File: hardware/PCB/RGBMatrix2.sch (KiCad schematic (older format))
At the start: 29 parts

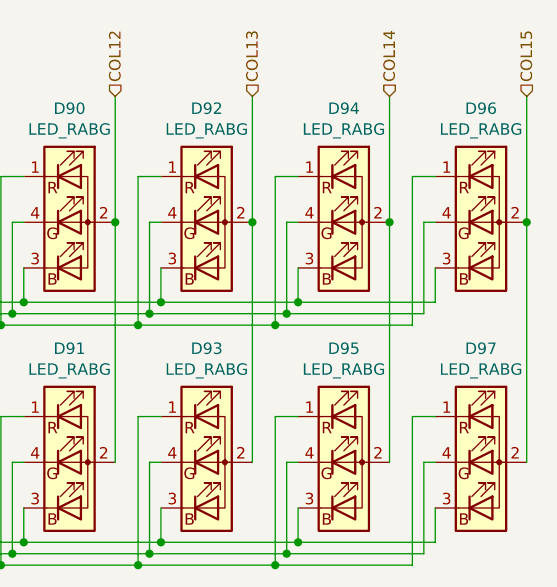
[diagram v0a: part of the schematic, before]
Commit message: Line up most parts and fix some problems with the part
1.Fix the LED footprint size
2.Edit the hotplug to be simpler (removed 2 holes)
3.Line up everything and the silkscreen
4. Fix the LED matrix and the switch matrix sch
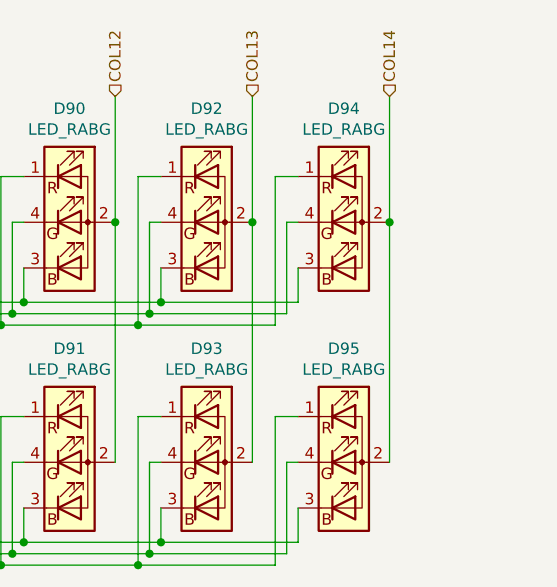
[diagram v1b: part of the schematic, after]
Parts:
- removed D96, D97: LED_RABG, KiCad:XZMDKCBDDG45S9, symbol Device:LED_RABG
- D69, D70, D71, D72, D73, D74, D75, D76, D77, D78, D79, D80, D81, D82, D83, D84, D85, D86, D87, D88, D89, D90, D91, D92, D93, D94, D95: footprint KiCad:XZMDKCBDDG45S9 -> KiCad:XZMDKCBDDG45S9_fixed

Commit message: alot of changes
modify the QFN-48 so PCB 3d view in future would look better (so I don't design a part that doesn't fit)
I made a useless QFN-40 3d model
modify schematics so it looks better
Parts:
- D69, D70, D71, D72, D73, D74, D75, D76, D77, D78, D79, D80, D81, D82, D83, D84, D85, D86, D87, D88, D89, D90, D91, D92, D93, D94, D95: Footprint (none) -> KiCad:XZMDKCBDDG45S9_fixed; Value (none) -> XZMDKCBDDG45S9
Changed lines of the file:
@@
 encoding utf-8
 Sheet 4 6
-Title ""
-Date ""
-Rev ""
+Title "NHW68"
+Date "2020-01-28"
+Rev "0.1"
 Comp ""
 Comment1 ""
@@
 F 2 "KiCad:XZMDKCBDDG45S9_fixed" H 1750 2350 50  0001 C CNN
 F 3 "~" H 1750 2350 50  0001 C CNN
+F 4 "KiCad:XZMDKCBDDG45S9_fixed" H 1750 2400 50  0001 C CNN "Footprint"
+F 5 "XZMDKCBDDG45S9" H 1750 2400 50  0001 C CNN "Value"
 	1    1750 2400
 	1    0    0    -1
@@
 F 2 "KiCad:XZMDKCBDDG45S9_fixed" H 2350 2350 50  0001 C CNN
 F 3 "~" H 2350 2350 50  0001 C CNN
+F 4 "KiCad:XZMDKCBDDG45S9_fixed" H 2350 2400 50  0001 C CNN "Footprint"
+F 5 "XZMDKCBDDG45S9" H 2350 2400 50  0001 C CNN "Value"
 	1    2350 2400
 	1    0    0    -1
@@
 F 2 "KiCad:XZMDKCBDDG45S9_fixed" H 2950 2350 50  0001 C CNN
 F 3 "~" H 2950 2350 50  0001 C CNN
+F 4 "KiCad:XZMDKCBDDG45S9_fixed" H 2950 2400 50  0001 C CNN "Footprint"
+F 5 "XZMDKCBDDG45S9" H 2950 2400 50  0001 C CNN "Value"
 	1    2950 2400
 	1    0    0    -1
@@
 F 2 "KiCad:XZMDKCBDDG45S9_fixed" H 3550 2350 50  0001 C CNN
 F 3 "~" H 3550 2350 50  0001 C CNN
+F 4 "KiCad:XZMDKCBDDG45S9_fixed" H 3550 2400 50  0001 C CNN "Footprint"
+F 5 "XZMDKCBDDG45S9" H 3550 2400 50  0001 C CNN "Value"
 	1    3550 2400
 	1    0    0    -1
@@
 F 2 "KiCad:XZMDKCBDDG45S9_fixed" H 4100 2350 50  0001 C CNN
 F 3 "~" H 4100 2350 50  0001 C CNN
+F 4 "KiCad:XZMDKCBDDG45S9_fixed" H 4100 2400 50  0001 C CNN "Footprint"
+F 5 "XZMDKCBDDG45S9" H 4100 2400 50  0001 C CNN "Value"
 	1    4100 2400
 	1    0    0    -1
@@
 F 2 "KiCad:XZMDKCBDDG45S9_fixed" H 4700 2350 50  0001 C CNN
 F 3 "~" H 4700 2350 50  0001 C CNN
+F 4 "KiCad:XZMDKCBDDG45S9_fixed" H 4700 2400 50  0001 C CNN "Footprint"
+F 5 "XZMDKCBDDG45S9" H 4700 2400 50  0001 C CNN "Value"
 	1    4700 2400
 	1    0    0    -1
@@
 F 2 "KiCad:XZMDKCBDDG45S9_fixed" H 5300 2350 50  0001 C CNN
 F 3 "~" H 5300 2350 50  0001 C CNN
+F 4 "KiCad:XZMDKCBDDG45S9_fixed" H 5300 2400 50  0001 C CNN "Footprint"
+F 5 "XZMDKCBDDG45S9" H 5300 2400 50  0001 C CNN "Value"
 	1    5300 2400
 	1    0    0    -1
@@
 F 2 "KiCad:XZMDKCBDDG45S9_fixed" H 5900 2350 50  0001 C CNN
 F 3 "~" H 5900 2350 50  0001 C CNN
+F 4 "KiCad:XZMDKCBDDG45S9_fixed" H 5900 2400 50  0001 C CNN "Footprint"
+F 5 "XZMDKCBDDG45S9" H 5900 2400 50  0001 C CNN "Value"
 	1    5900 2400
 	1    0    0    -1
@@
 F 2 "KiCad:XZMDKCBDDG45S9_fixed" H 6500 2350 50  0001 C CNN
 F 3 "~" H 6500 2350 50  0001 C CNN
+F 4 "KiCad:XZMDKCBDDG45S9_fixed" H 6500 2400 50  0001 C CNN "Footprint"
+F 5 "XZMDKCBDDG45S9" H 6500 2400 50  0001 C CNN "Value"
 	1    6500 2400
 	1    0    0    -1
@@
 F 2 "KiCad:XZMDKCBDDG45S9_fixed" H 7100 2350 50  0001 C CNN
 F 3 "~" H 7100 2350 50  0001 C CNN
+F 4 "KiCad:XZMDKCBDDG45S9_fixed" H 7100 2400 50  0001 C CNN "Footprint"
+F 5 "XZMDKCBDDG45S9" H 7100 2400 50  0001 C CNN "Value"
 	1    7100 2400
 	1    0    0    -1
@@
 F 2 "KiCad:XZMDKCBDDG45S9_fixed" H 7700 2350 50  0001 C CNN
 F 3 "~" H 7700 2350 50  0001 C CNN
+F 4 "KiCad:XZMDKCBDDG45S9_fixed" H 7700 2400 50  0001 C CNN "Footprint"
+F 5 "XZMDKCBDDG45S9" H 7700 2400 50  0001 C CNN "Value"
 	1    7700 2400
 	1    0    0    -1
@@
 F 2 "KiCad:XZMDKCBDDG45S9_fixed" H 8300 2350 50  0001 C CNN
 F 3 "~" H 8300 2350 50  0001 C CNN
+F 4 "KiCad:XZMDKCBDDG45S9_fixed" H 8300 2400 50  0001 C CNN "Footprint"
+F 5 "XZMDKCBDDG45S9" H 8300 2400 50  0001 C CNN "Value"
 	1    8300 2400
 	1    0    0    -1
@@
 F 2 "KiCad:XZMDKCBDDG45S9_fixed" H 8900 2350 50  0001 C CNN
 F 3 "~" H 8900 2350 50  0001 C CNN
+F 4 "KiCad:XZMDKCBDDG45S9_fixed" H 8900 2400 50  0001 C CNN "Footprint"
+F 5 "XZMDKCBDDG45S9" H 8900 2400 50  0001 C CNN "Value"
 	1    8900 2400
 	1    0    0    -1
@@
 F 2 "KiCad:XZMDKCBDDG45S9_fixed" H 9500 2350 50  0001 C CNN
 F 3 "~" H 9500 2350 50  0001 C CNN
+F 4 "KiCad:XZMDKCBDDG45S9_fixed" H 9500 2400 50  0001 C CNN "Footprint"
+F 5 "XZMDKCBDDG45S9" H 9500 2400 50  0001 C CNN "Value"
 	1    9500 2400
 	1    0    0    -1
@@
 F 2 "KiCad:XZMDKCBDDG45S9_fixed" H 9500 3400 50  0001 C CNN
 F 3 "~" H 9500 3400 50  0001 C CNN
+F 4 "KiCad:XZMDKCBDDG45S9_fixed" H 9500 3450 50  0001 C CNN "Footprint"
+F 5 "XZMDKCBDDG45S9" H 9500 3450 50  0001 C CNN "Value"
 	1    9500 3450
 	1    0    0    -1
@@
 F 2 "KiCad:XZMDKCBDDG45S9_fixed" H 8300 3400 50  0001 C CNN
 F 3 "~" H 8300 3400 50  0001 C CNN
+F 4 "KiCad:XZMDKCBDDG45S9_fixed" H 8300 3450 50  0001 C CNN "Footprint"
+F 5 "XZMDKCBDDG45S9" H 8300 3450 50  0001 C CNN "Value"
 	1    8300 3450
 	1    0    0    -1
@@
 F 2 "KiCad:XZMDKCBDDG45S9_fixed" H 7700 3400 50  0001 C CNN
 F 3 "~" H 7700 3400 50  0001 C CNN
+F 4 "KiCad:XZMDKCBDDG45S9_fixed" H 7700 3450 50  0001 C CNN "Footprint"
+F 5 "XZMDKCBDDG45S9" H 7700 3450 50  0001 C CNN "Value"
 	1    7700 3450
 	1    0    0    -1
@@
 F 2 "KiCad:XZMDKCBDDG45S9_fixed" H 7100 3400 50  0001 C CNN
 F 3 "~" H 7100 3400 50  0001 C CNN
+F 4 "KiCad:XZMDKCBDDG45S9_fixed" H 7100 3450 50  0001 C CNN "Footprint"
+F 5 "XZMDKCBDDG45S9" H 7100 3450 50  0001 C CNN "Value"
 	1    7100 3450
 	1    0    0    -1
@@
 F 2 "KiCad:XZMDKCBDDG45S9_fixed" H 6500 3400 50  0001 C CNN
 F 3 "~" H 6500 3400 50  0001 C CNN
+F 4 "KiCad:XZMDKCBDDG45S9_fixed" H 6500 3450 50  0001 C CNN "Footprint"
+F 5 "XZMDKCBDDG45S9" H 6500 3450 50  0001 C CNN "Value"
 	1    6500 3450
 	1    0    0    -1
@@
 F 2 "KiCad:XZMDKCBDDG45S9_fixed" H 5900 3400 50  0001 C CNN
 F 3 "~" H 5900 3400 50  0001 C CNN
+F 4 "KiCad:XZMDKCBDDG45S9_fixed" H 5900 3450 50  0001 C CNN "Footprint"
+F 5 "XZMDKCBDDG45S9" H 5900 3450 50  0001 C CNN "Value"
 	1    5900 3450
 	1    0    0    -1
@@
 F 2 "KiCad:XZMDKCBDDG45S9_fixed" H 4700 3400 50  0001 C CNN
 F 3 "~" H 4700 3400 50  0001 C CNN
+F 4 "KiCad:XZMDKCBDDG45S9_fixed" H 4700 3450 50  0001 C CNN "Footprint"
+F 5 "XZMDKCBDDG45S9" H 4700 3450 50  0001 C CNN "Value"
 	1    4700 3450
 	1    0    0    -1
@@
 F 2 "KiCad:XZMDKCBDDG45S9_fixed" H 4100 3400 50  0001 C CNN
 F 3 "~" H 4100 3400 50  0001 C CNN
+F 4 "KiCad:XZMDKCBDDG45S9_fixed" H 4100 3450 50  0001 C CNN "Footprint"
+F 5 "XZMDKCBDDG45S9" H 4100 3450 50  0001 C CNN "Value"
 	1    4100 3450
 	1    0    0    -1
@@
 F 2 "KiCad:XZMDKCBDDG45S9_fixed" H 3550 3400 50  0001 C CNN
 F 3 "~" H 3550 3400 50  0001 C CNN
+F 4 "KiCad:XZMDKCBDDG45S9_fixed" H 3550 3450 50  0001 C CNN "Footprint"
+F 5 "XZMDKCBDDG45S9" H 3550 3450 50  0001 C CNN "Value"
 	1    3550 3450
 	1    0    0    -1
@@
 F 2 "KiCad:XZMDKCBDDG45S9_fixed" H 2950 3400 50  0001 C CNN
 F 3 "~" H 2950 3400 50  0001 C CNN
+F 4 "KiCad:XZMDKCBDDG45S9_fixed" H 2950 3450 50  0001 C CNN "Footprint"
+F 5 "XZMDKCBDDG45S9" H 2950 3450 50  0001 C CNN "Value"
 	1    2950 3450
 	1    0    0    -1
@@
 F 2 "KiCad:XZMDKCBDDG45S9_fixed" H 2350 3400 50  0001 C CNN
 F 3 "~" H 2350 3400 50  0001 C CNN
+F 4 "KiCad:XZMDKCBDDG45S9_fixed" H 2350 3450 50  0001 C CNN "Footprint"
+F 5 "XZMDKCBDDG45S9" H 2350 3450 50  0001 C CNN "Value"
 	1    2350 3450
 	1    0    0    -1
@@
 F 2 "KiCad:XZMDKCBDDG45S9_fixed" H 1750 3400 50  0001 C CNN
 F 3 "~" H 1750 3400 50  0001 C CNN
+F 4 "KiCad:XZMDKCBDDG45S9_fixed" H 1750 3450 50  0001 C CNN "Footprint"
+F 5 "XZMDKCBDDG45S9" H 1750 3450 50  0001 C CNN "Value"
 	1    1750 3450
 	1    0    0    -1
@@
 F 2 "KiCad:XZMDKCBDDG45S9_fixed" H 8900 3400 50  0001 C CNN
 F 3 "~" H 8900 3400 50  0001 C CNN
+F 4 "KiCad:XZMDKCBDDG45S9_fixed" H 8900 3450 50  0001 C CNN "Footprint"
+F 5 "XZMDKCBDDG45S9" H 8900 3450 50  0001 C CNN "Value"
 	1    8900 3450
 	1    0    0    -1

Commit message: making progress
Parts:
- D69, D70, D71, D72, D73, D74, D75, D76, D77, D78, D79, D80, D81, D82, D83, D84, D85, D86, D87, D88, D89, D90, D91, D92, D93, D94, D95: value LED_RABG -> XZMDKCBDDG45S-9
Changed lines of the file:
@@
 AR Path="/5EC33E3D/5E12F961/5ECE6F4E" Ref="D69"  Part="1"
 F 0 "D69" H 1750 2897 50  0000 C CNN
-F 1 "LED_RABG" H 1750 2806 50  0000 C CNN
+F 1 "XZMDKCBDDG45S-9" H 1750 2806 50  0000 C CNN
 F 2 "KiCad:XZMDKCBDDG45S9_fixed" H 1750 2350 50  0001 C CNN
 F 3 "~" H 1750 2350 50  0001 C CNN
@@
 AR Path="/5EC33E3D/5E12F961/5ECF7D8D" Ref="D71"  Part="1"
 F 0 "D71" H 2350 2897 50  0000 C CNN
-F 1 "LED_RABG" H 2350 2806 50  0000 C CNN
+F 1 "XZMDKCBDDG45S-9" H 2350 2806 50  0000 C CNN
 F 2 "KiCad:XZMDKCBDDG45S9_fixed" H 2350 2350 50  0001 C CNN
 F 3 "~" H 2350 2350 50  0001 C CNN
@@
 AR Path="/5EC33E3D/5E12F961/5ED08C1C" Ref="D73"  Part="1"
 F 0 "D73" H 2950 2897 50  0000 C CNN
-F 1 "LED_RABG" H 2950 2806 50  0000 C CNN
+F 1 "XZMDKCBDDG45S-9" H 2950 2806 50  0000 C CNN
 F 2 "KiCad:XZMDKCBDDG45S9_fixed" H 2950 2350 50  0001 C CNN
 F 3 "~" H 2950 2350 50  0001 C CNN
@@
 AR Path="/5EC33E3D/5E12F961/5ED19532" Ref="D75"  Part="1"
 F 0 "D75" H 3550 2897 50  0000 C CNN
-F 1 "LED_RABG" H 3550 2806 50  0000 C CNN
+F 1 "XZMDKCBDDG45S-9" H 3550 2806 50  0000 C CNN
 F 2 "KiCad:XZMDKCBDDG45S9_fixed" H 3550 2350 50  0001 C CNN
 F 3 "~" H 3550 2350 50  0001 C CNN
@@
 AR Path="/5EC33E3D/5E12F961/5ED2A1D2" Ref="D77"  Part="1"
 F 0 "D77" H 4100 2897 50  0000 C CNN
-F 1 "LED_RABG" H 4100 2806 50  0000 C CNN
+F 1 "XZMDKCBDDG45S-9" H 4100 2806 50  0000 C CNN
 F 2 "KiCad:XZMDKCBDDG45S9_fixed" H 4100 2350 50  0001 C CNN
 F 3 "~" H 4100 2350 50  0001 C CNN
@@
 AR Path="/5EC33E3D/5E12F961/5ED3AE35" Ref="D79"  Part="1"
 F 0 "D79" H 4700 2897 50  0000 C CNN
-F 1 "LED_RABG" H 4700 2806 50  0000 C CNN
+F 1 "XZMDKCBDDG45S-9" H 4700 2806 50  0000 C CNN
 F 2 "KiCad:XZMDKCBDDG45S9_fixed" H 4700 2350 50  0001 C CNN
 F 3 "~" H 4700 2350 50  0001 C CNN
@@
 AR Path="/5EC33E3D/5E12F961/5ED4B8F9" Ref="D81"  Part="1"
 F 0 "D81" H 5300 2897 50  0000 C CNN
-F 1 "LED_RABG" H 5300 2806 50  0000 C CNN
+F 1 "XZMDKCBDDG45S-9" H 5300 2806 50  0000 C CNN
 F 2 "KiCad:XZMDKCBDDG45S9_fixed" H 5300 2350 50  0001 C CNN
 F 3 "~" H 5300 2350 50  0001 C CNN
@@
 AR Path="/5EC33E3D/5E12F961/5ED5C37B" Ref="D82"  Part="1"
 F 0 "D82" H 5900 2897 50  0000 C CNN
-F 1 "LED_RABG" H 5900 2806 50  0000 C CNN
+F 1 "XZMDKCBDDG45S-9" H 5900 2806 50  0000 C CNN
 F 2 "KiCad:XZMDKCBDDG45S9_fixed" H 5900 2350 50  0001 C CNN
 F 3 "~" H 5900 2350 50  0001 C CNN
@@
 AR Path="/5EC33E3D/5E12F961/5ED6CA4B" Ref="D84"  Part="1"
 F 0 "D84" H 6500 2897 50  0000 C CNN
-F 1 "LED_RABG" H 6500 2806 50  0000 C CNN
+F 1 "XZMDKCBDDG45S-9" H 6500 2806 50  0000 C CNN
 F 2 "KiCad:XZMDKCBDDG45S9_fixed" H 6500 2350 50  0001 C CNN
 F 3 "~" H 6500 2350 50  0001 C CNN
@@
 AR Path="/5EC33E3D/5E12F961/5ED7D671" Ref="D86"  Part="1"
 F 0 "D86" H 7100 2897 50  0000 C CNN
-F 1 "LED_RABG" H 7100 2806 50  0000 C CNN
+F 1 "XZMDKCBDDG45S-9" H 7100 2806 50  0000 C CNN
 F 2 "KiCad:XZMDKCBDDG45S9_fixed" H 7100 2350 50  0001 C CNN
 F 3 "~" H 7100 2350 50  0001 C CNN
@@
 AR Path="/5EC33E3D/5E12F961/5ED8E3BC" Ref="D88"  Part="1"
 F 0 "D88" H 7700 2897 50  0000 C CNN
-F 1 "LED_RABG" H 7700 2806 50  0000 C CNN
+F 1 "XZMDKCBDDG45S-9" H 7700 2806 50  0000 C CNN
 F 2 "KiCad:XZMDKCBDDG45S9_fixed" H 7700 2350 50  0001 C CNN
 F 3 "~" H 7700 2350 50  0001 C CNN
@@
 AR Path="/5EC33E3D/5E12F961/5ED9EECC" Ref="D90"  Part="1"
 F 0 "D90" H 8300 2897 50  0000 C CNN
-F 1 "LED_RABG" H 8300 2806 50  0000 C CNN
+F 1 "XZMDKCBDDG45S-9" H 8300 2806 50  0000 C CNN
 F 2 "KiCad:XZMDKCBDDG45S9_fixed" H 8300 2350 50  0001 C CNN
 F 3 "~" H 8300 2350 50  0001 C CNN
@@
 AR Path="/5EC33E3D/5E12F961/5EDAF8D0" Ref="D92"  Part="1"
 F 0 "D92" H 8900 2897 50  0000 C CNN
-F 1 "LED_RABG" H 8900 2806 50  0000 C CNN
+F 1 "XZMDKCBDDG45S-9" H 8900 2806 50  0000 C CNN
 F 2 "KiCad:XZMDKCBDDG45S9_fixed" H 8900 2350 50  0001 C CNN
 F 3 "~" H 8900 2350 50  0001 C CNN
@@
 AR Path="/5EC33E3D/5E12F961/5EDC0468" Ref="D94"  Part="1"
 F 0 "D94" H 9500 2897 50  0000 C CNN
-F 1 "LED_RABG" H 9500 2806 50  0000 C CNN
+F 1 "XZMDKCBDDG45S-9" H 9500 2806 50  0000 C CNN
 F 2 "KiCad:XZMDKCBDDG45S9_fixed" H 9500 2350 50  0001 C CNN
 F 3 "~" H 9500 2350 50  0001 C CNN
@@
 AR Path="/5EC33E3D/5E12F961/5EDF2634" Ref="D95"  Part="1"
 F 0 "D95" H 9500 3947 50  0000 C CNN
-F 1 "LED_RABG" H 9500 3856 50  0000 C CNN
+F 1 "XZMDKCBDDG45S-9" H 9500 3856 50  0000 C CNN
 F 2 "KiCad:XZMDKCBDDG45S9_fixed" H 9500 3400 50  0001 C CNN
 F 3 "~" H 9500 3400 50  0001 C CNN
@@
 AR Path="/5EC33E3D/5E12F961/5EE13AA6" Ref="D91"  Part="1"
 F 0 "D91" H 8300 3947 50  0000 C CNN
-F 1 "LED_RABG" H 8300 3856 50  0000 C CNN
+F 1 "XZMDKCBDDG45S-9" H 8300 3856 50  0000 C CNN
 F 2 "KiCad:XZMDKCBDDG45S9_fixed" H 8300 3400 50  0001 C CNN
 F 3 "~" H 8300 3400 50  0001 C CNN
@@
 AR Path="/5EC33E3D/5E12F961/5EE24547" Ref="D89"  Part="1"
 F 0 "D89" H 7700 3947 50  0000 C CNN
-F 1 "LED_RABG" H 7700 3856 50  0000 C CNN
+F 1 "XZMDKCBDDG45S-9" H 7700 3856 50  0000 C CNN
 F 2 "KiCad:XZMDKCBDDG45S9_fixed" H 7700 3400 50  0001 C CNN
 F 3 "~" H 7700 3400 50  0001 C CNN
@@
 AR Path="/5EC33E3D/5E12F961/5EE34C17" Ref="D87"  Part="1"
 F 0 "D87" H 7100 3947 50  0000 C CNN
-F 1 "LED_RABG" H 7100 3856 50  0000 C CNN
+F 1 "XZMDKCBDDG45S-9" H 7100 3856 50  0000 C CNN
 F 2 "KiCad:XZMDKCBDDG45S9_fixed" H 7100 3400 50  0001 C CNN
 F 3 "~" H 7100 3400 50  0001 C CNN
@@
 AR Path="/5EC33E3D/5E12F961/5EE45875" Ref="D85"  Part="1"
 F 0 "D85" H 6500 3947 50  0000 C CNN
-F 1 "LED_RABG" H 6500 3856 50  0000 C CNN
+F 1 "XZMDKCBDDG45S-9" H 6500 3856 50  0000 C CNN
 F 2 "KiCad:XZMDKCBDDG45S9_fixed" H 6500 3400 50  0001 C CNN
 F 3 "~" H 6500 3400 50  0001 C CNN
@@
 AR Path="/5EC33E3D/5E12F961/5EE56B5B" Ref="D83"  Part="1"
 F 0 "D83" H 5900 3947 50  0000 C CNN
-F 1 "LED_RABG" H 5900 3856 50  0000 C CNN
+F 1 "XZMDKCBDDG45S-9" H 5900 3856 50  0000 C CNN
 F 2 "KiCad:XZMDKCBDDG45S9_fixed" H 5900 3400 50  0001 C CNN
 F 3 "~" H 5900 3400 50  0001 C CNN
@@
 AR Path="/5EC33E3D/5E12F961/5EE68DA5" Ref="D80"  Part="1"
 F 0 "D80" H 4700 3947 50  0000 C CNN
-F 1 "LED_RABG" H 4700 3856 50  0000 C CNN
+F 1 "XZMDKCBDDG45S-9" H 4700 3856 50  0000 C CNN
 F 2 "KiCad:XZMDKCBDDG45S9_fixed" H 4700 3400 50  0001 C CNN
 F 3 "~" H 4700 3400 50  0001 C CNN
@@
 AR Path="/5EC33E3D/5E12F961/5EE797FA" Ref="D78"  Part="1"
 F 0 "D78" H 4100 3947 50  0000 C CNN
-F 1 "LED_RABG" H 4100 3856 50  0000 C CNN
+F 1 "XZMDKCBDDG45S-9" H 4100 3856 50  0000 C CNN
 F 2 "KiCad:XZMDKCBDDG45S9_fixed" H 4100 3400 50  0001 C CNN
 F 3 "~" H 4100 3400 50  0001 C CNN
@@
 AR Path="/5EC33E3D/5E12F961/5EE8A2F6" Ref="D76"  Part="1"
 F 0 "D76" H 3550 3947 50  0000 C CNN
-F 1 "LED_RABG" H 3550 3856 50  0000 C CNN
+F 1 "XZMDKCBDDG45S-9" H 3550 3856 50  0000 C CNN
 F 2 "KiCad:XZMDKCBDDG45S9_fixed" H 3550 3400 50  0001 C CNN
 F 3 "~" H 3550 3400 50  0001 C CNN
@@
 AR Path="/5EC33E3D/5E12F961/5EEAC0EB" Ref="D74"  Part="1"
 F 0 "D74" H 2950 3947 50  0000 C CNN
-F 1 "LED_RABG" H 2950 3856 50  0000 C CNN
+F 1 "XZMDKCBDDG45S-9" H 2950 3856 50  0000 C CNN
 F 2 "KiCad:XZMDKCBDDG45S9_fixed" H 2950 3400 50  0001 C CNN
 F 3 "~" H 2950 3400 50  0001 C CNN
@@
 AR Path="/5EC33E3D/5E12F961/5EEBC7BB" Ref="D72"  Part="1"
 F 0 "D72" H 2350 3947 50  0000 C CNN
-F 1 "LED_RABG" H 2350 3856 50  0000 C CNN
+F 1 "XZMDKCBDDG45S-9" H 2350 3856 50  0000 C CNN
 F 2 "KiCad:XZMDKCBDDG45S9_fixed" H 2350 3400 50  0001 C CNN
 F 3 "~" H 2350 3400 50  0001 C CNN
@@
 AR Path="/5EC33E3D/5E12F961/5EECD5B2" Ref="D70"  Part="1"
 F 0 "D70" H 1750 3947 50  0000 C CNN
-F 1 "LED_RABG" H 1750 3856 50  0000 C CNN
+F 1 "XZMDKCBDDG45S-9" H 1750 3856 50  0000 C CNN
 F 2 "KiCad:XZMDKCBDDG45S9_fixed" H 1750 3400 50  0001 C CNN
 F 3 "~" H 1750 3400 50  0001 C CNN
@@
 AR Path="/5EC33E3D/5E12F961/5EE030A2" Ref="D93"  Part="1"
 F 0 "D93" H 8900 3947 50  0000 C CNN
-F 1 "LED_RABG" H 8900 3856 50  0000 C CNN
+F 1 "XZMDKCBDDG45S-9" H 8900 3856 50  0000 C CNN
 F 2 "KiCad:XZMDKCBDDG45S9_fixed" H 8900 3400 50  0001 C CNN
 F 3 "~" H 8900 3400 50  0001 C CNN
